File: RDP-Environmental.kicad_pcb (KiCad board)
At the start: 2 copper layers, 71.1 x 49.5 mm, 40 parts, among them J1 OPENLOG, J2 MPU, J3 RT1, J4 RT2, J5 RT3, J6 RT4, J7 3.3V, J8 AVR-PDI-6, U1 MS5607, U2 ATxmega32A4U-AU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

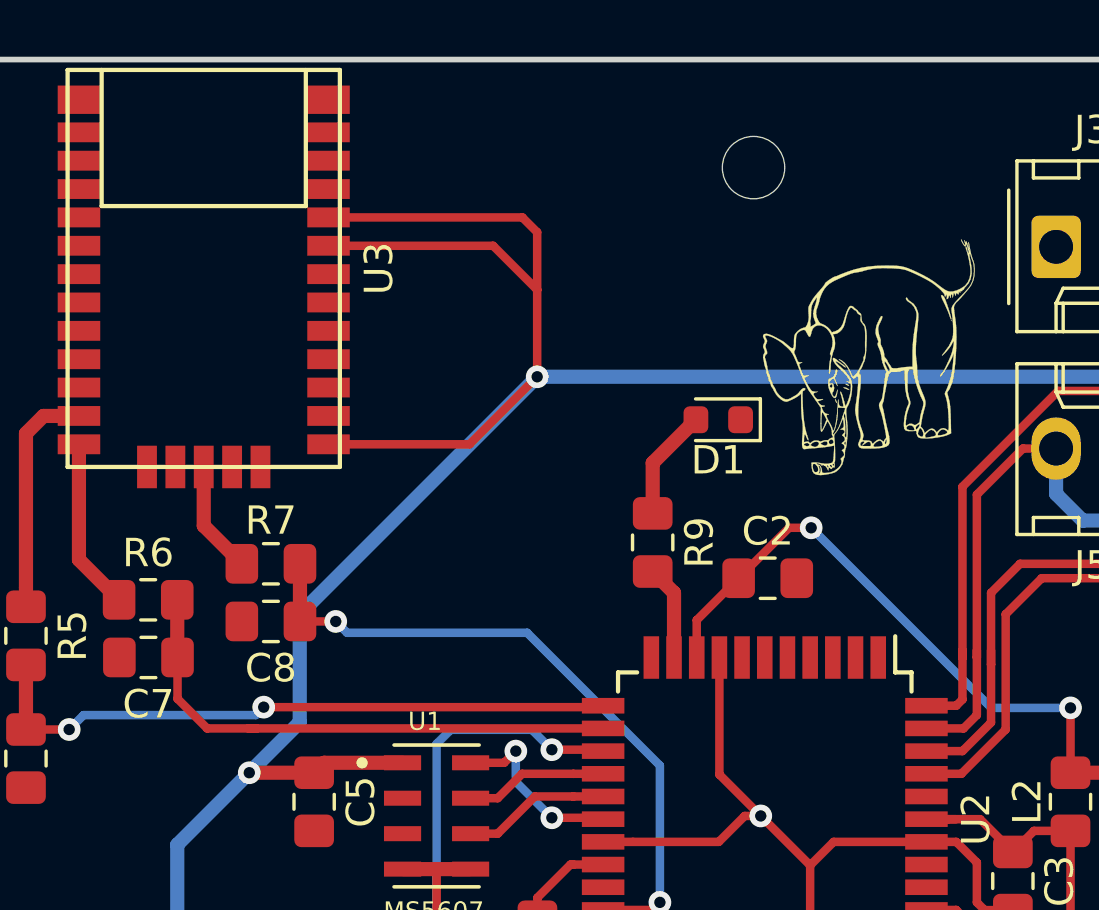
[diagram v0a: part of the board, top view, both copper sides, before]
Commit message: Add GPS and groud to output for FPGA
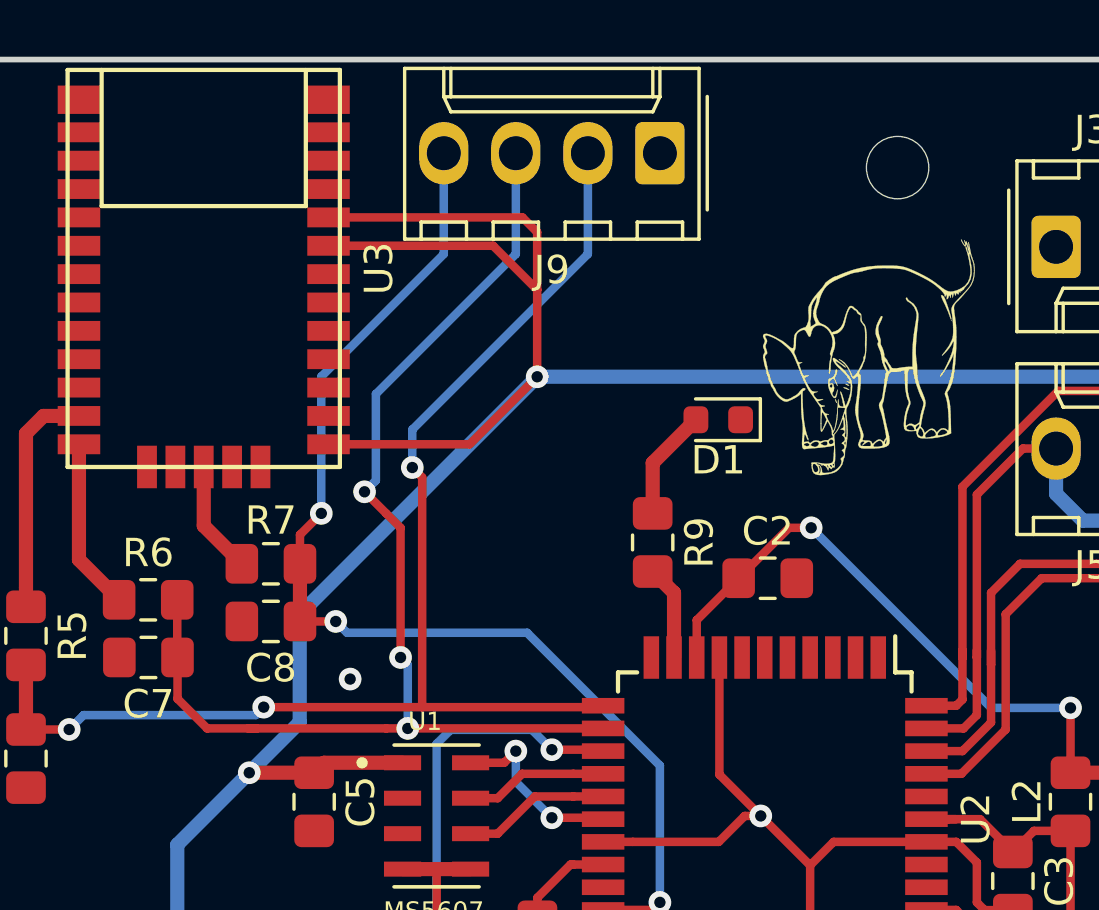
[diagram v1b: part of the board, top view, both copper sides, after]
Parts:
- added J9: FPGAO, Connector_Molex:Molex_KK-254_AE-6410-04A_1x04_P2.54mm_Vertical, F.Cu at (52.6, 24.9)
- moved REF** 5.08 mm to (61.0, 25.4)
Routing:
- net /TXC: track 19.2 -> 42.3 mm, vias 0 -> 3
- net /RXC: track 23.1 -> 45.3 mm, vias 2 -> 3
- net /PPS: track 23.8 -> 40.3 mm, vias 2 -> 3
- net GND: vias 1 -> 2
